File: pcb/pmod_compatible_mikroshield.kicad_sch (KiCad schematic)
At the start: 7 parts, among them J1 CON_HDR_MIKROBUS_ADDON_TH, J2 CON_HDR_100MILS_F_TH_RA_2X6, J3 CON_HDR_100MILS_M_TH_1X3, J4 CON_HDR_100MILS_M_TH_1X2, J5 CON_HDR_100MILS_M_TH_1X2

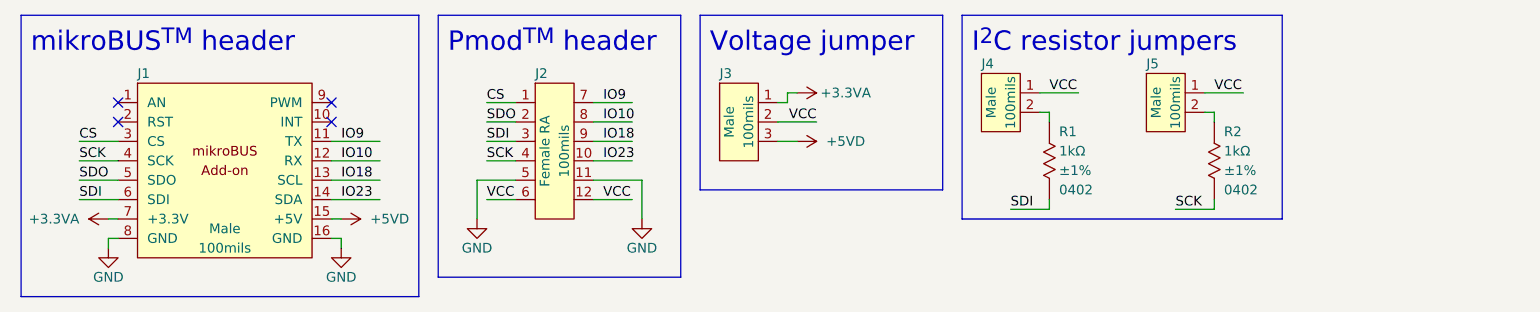
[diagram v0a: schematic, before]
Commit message: Fix name compliance with Pmod license Add RoHS logo Fix pin names
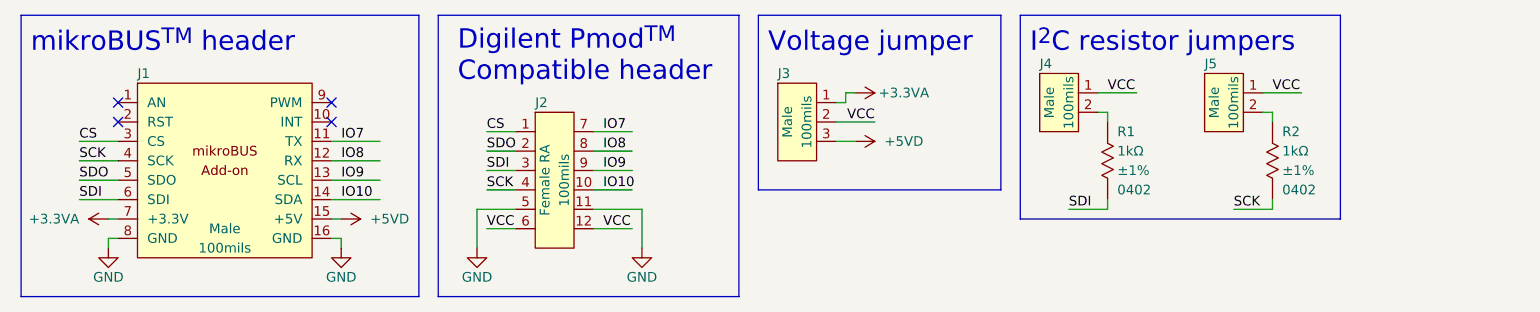
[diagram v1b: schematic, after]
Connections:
- net IO18 is gone; now on net IO9: J1.13 (SCL), J2.9
- net IO23 is gone; now on net IO10: J1.14 (SDA), J2.10
- net IO10: no longer J1.12 (RX), J2.8
- net IO9: no longer J1.11 (TX), J2.7
- new net IO7: J1.11 (TX), J2.7
- new net IO8: J1.12 (RX), J2.8
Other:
- note added: "Digilent Pmod^{TM} Compatible header"
- note removed: "Pmod^{TM} header"
- moved on the sheet: J2, J3, J4, J5, R1, R2

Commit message: Fix inverted SDO/SDI Add source resistors to signal lines
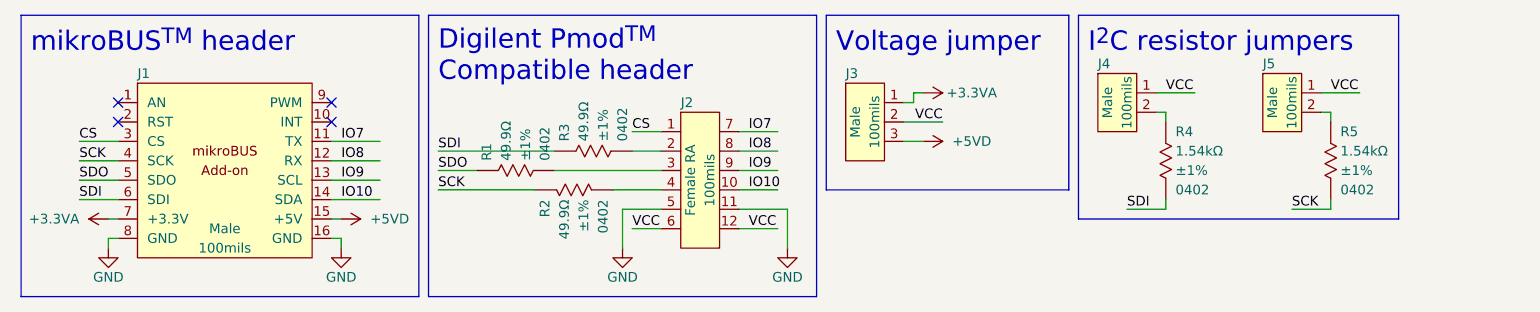
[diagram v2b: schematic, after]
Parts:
- added R1, R2, R3: RES_49.9Ω_1%_0402, connaxio-resistors:RES_0402_1005M, symbol connaxio-resistors:RES_49.9Ω_1%_0402
- R4: renamed from R1; value RES_1.00KΩ_1%_0402 -> RES_1.54KΩ_1%_0402; symbol connaxio-resistors:RES_1.00KΩ_1%_0402 -> connaxio-resistors:RES_1.54KΩ_1%_0402; Manufacturer Part Number RMCF0402FT1K00 -> RMCF0402FT1K54; Property 1kΩ -> 1.54kΩ
- R5: renamed from R2; value RES_1.00KΩ_1%_0402 -> RES_1.54KΩ_1%_0402; symbol connaxio-resistors:RES_1.00KΩ_1%_0402 -> connaxio-resistors:RES_1.54KΩ_1%_0402; Manufacturer Part Number RMCF0402FT1K00 -> RMCF0402FT1K54; Property 1kΩ -> 1.54kΩ
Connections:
- net SCK: now also R2.1; no longer J2.4
- net SDI: now also R3.1; no longer J2.3
- net SDO: now also R1.1; no longer J2.2
- new net: J2.2, R3.2
- new net: J2.3, R1.2
- new net: J2.4, R2.2
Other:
- moved on the sheet: J2, J3, J4, J5, R4, R5
